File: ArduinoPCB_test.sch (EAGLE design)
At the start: 17 parts, among them T1 2N4923

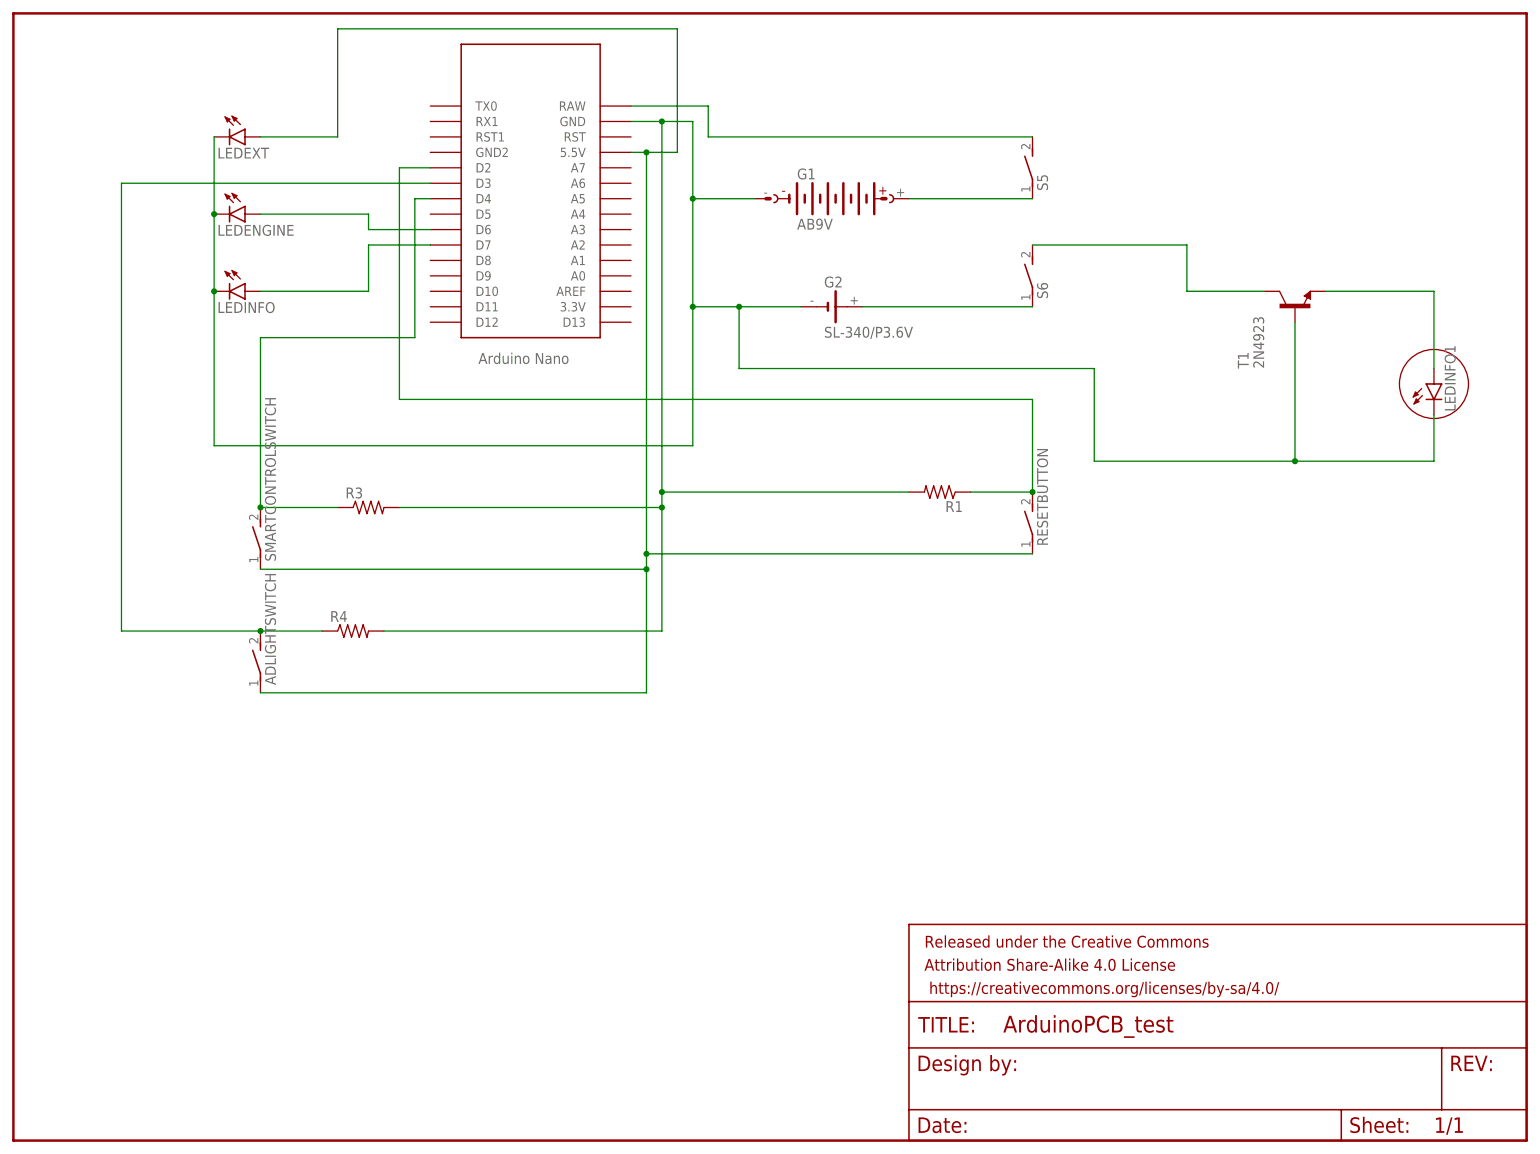
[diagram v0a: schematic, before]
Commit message: modifications made to ArduinoPCB_test
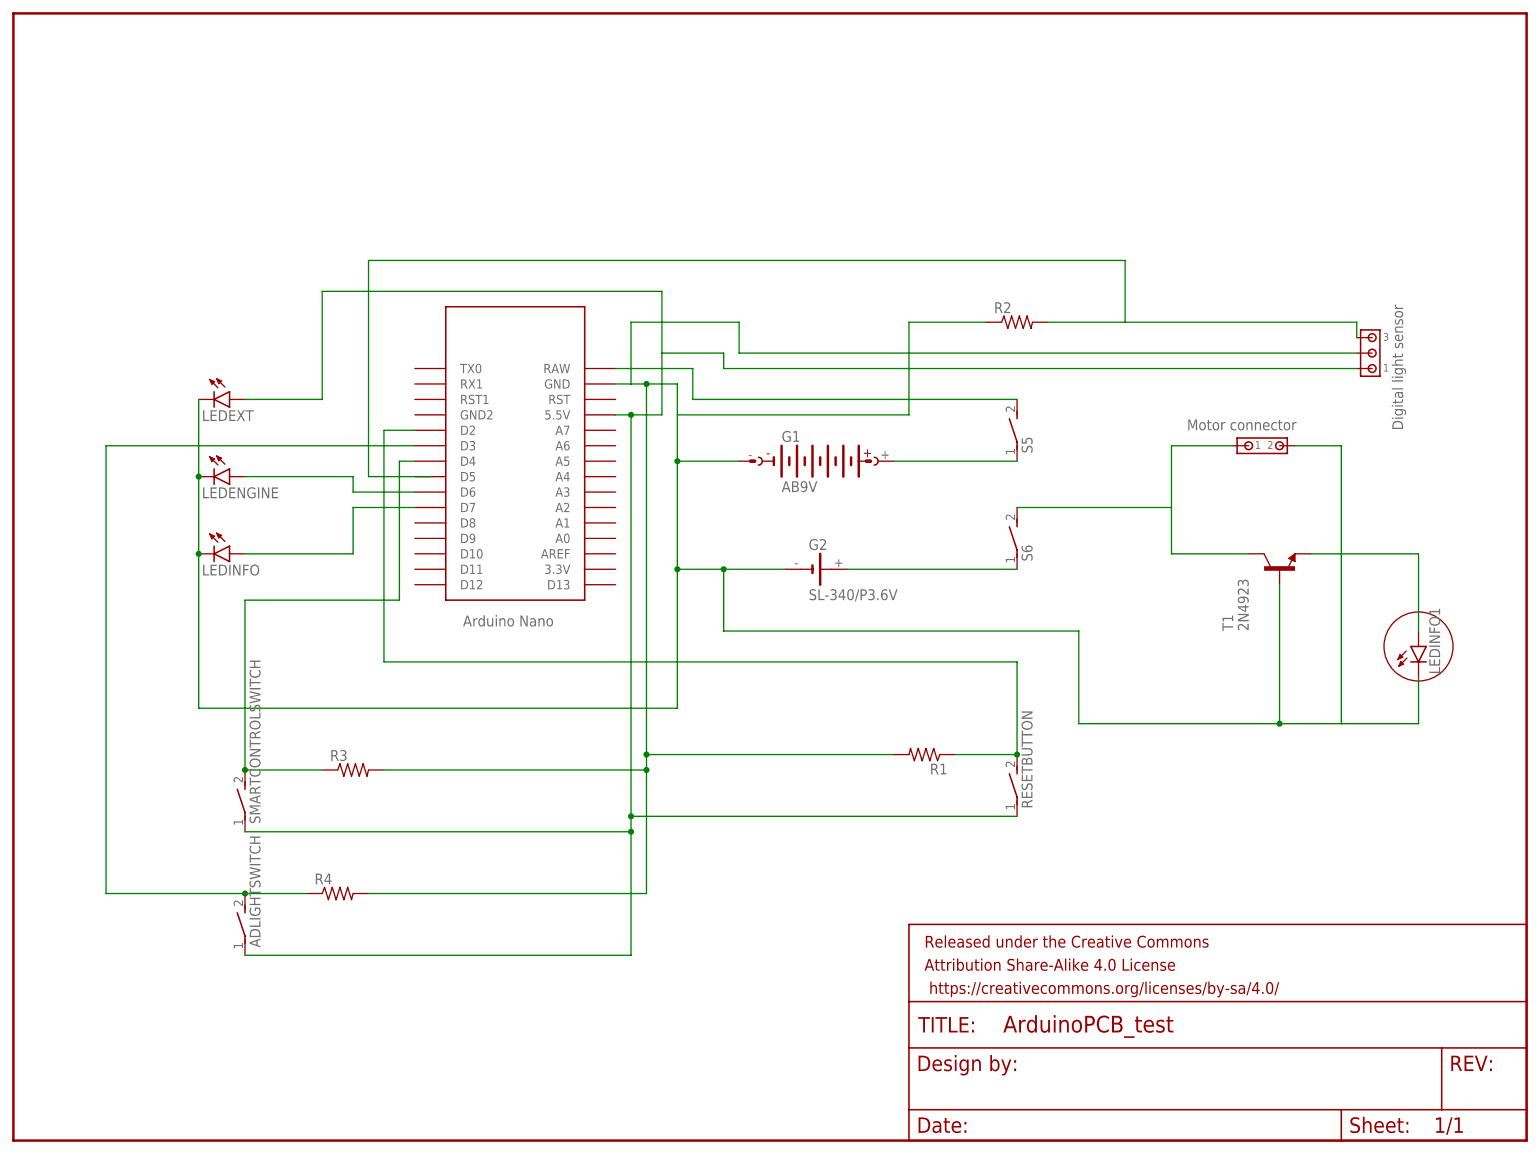
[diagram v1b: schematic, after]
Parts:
- added J1: 794681-2, con-amp:794681-2
- added J2: 1445055-3, con-amp:1445055-3
- added R2: (no value), rcl:R-US_0309/12
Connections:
- new net N$13: J2.3, R2.2
- net N$16: now also J1.1
- net N$8: now also J1.2, J2.2, R2.1
- net N$9: now also J2.1
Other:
- moved on the sheet: ADLIGHTSWITCH, G1, G2, LEDENGINE, LEDEXT, LEDINFO, LEDINFO1, R1, R3, R4, RESETBUTTON, S5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
